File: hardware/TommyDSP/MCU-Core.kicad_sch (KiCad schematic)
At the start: 35 parts, among them SW201 SW_Push, SW202 SW_Push, U201 W25Q128JVS, U202 DNF, U203 RP2350_60QFN, Y1 ABM8-272-T3

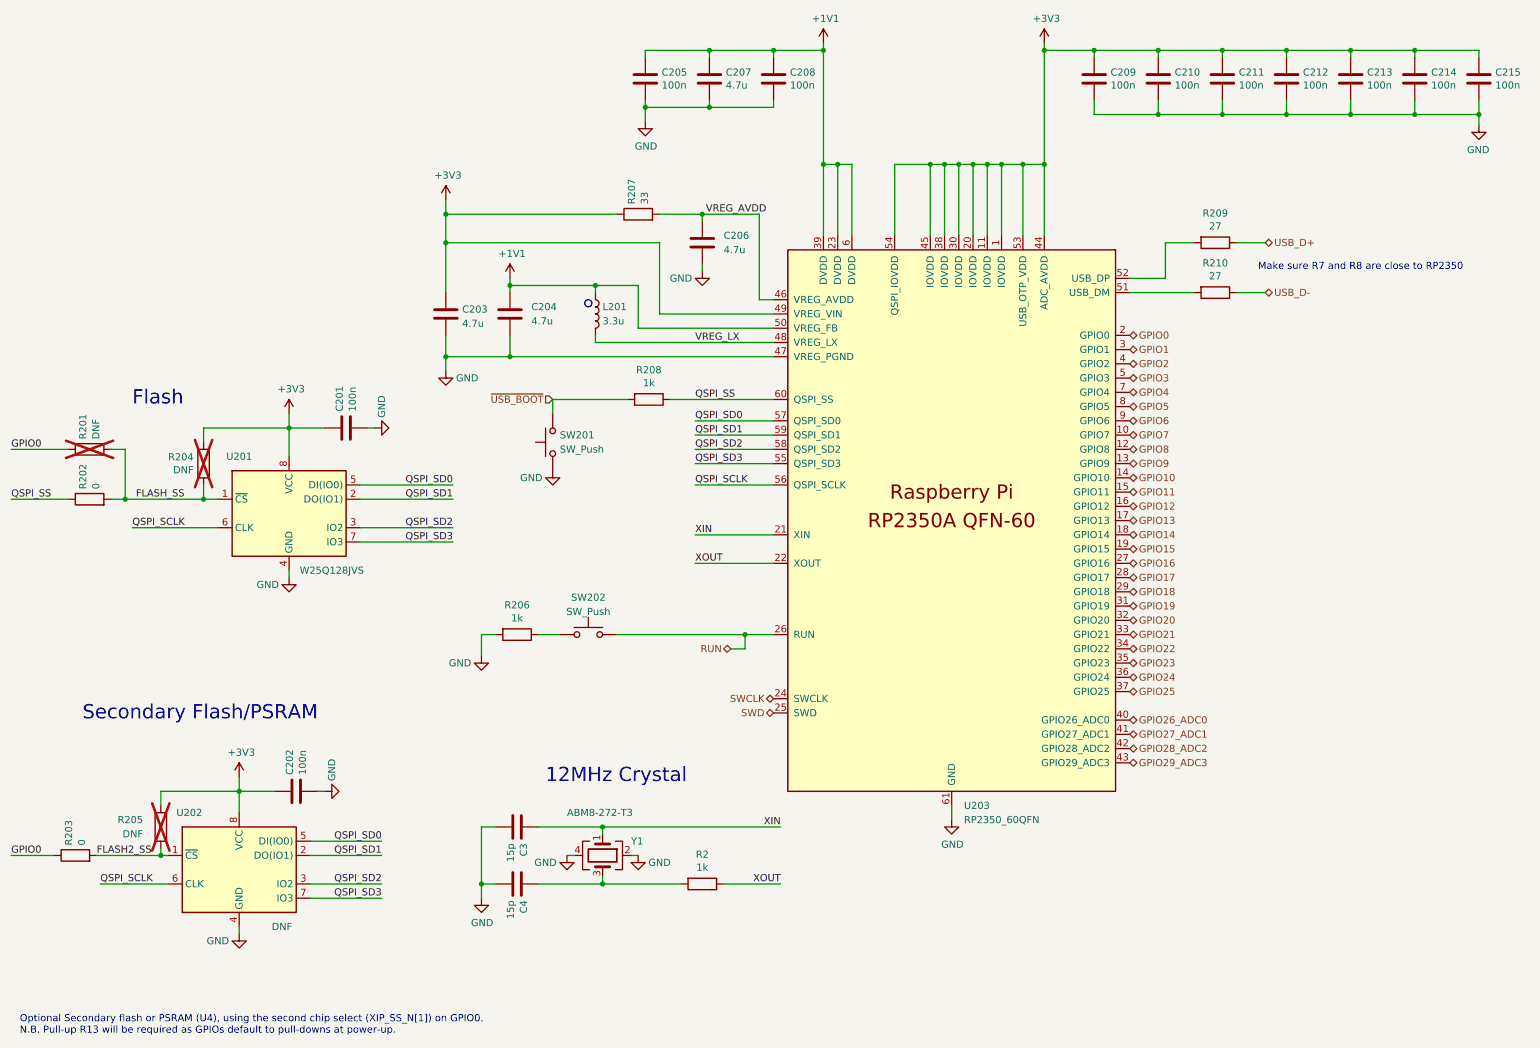
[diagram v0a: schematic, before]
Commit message: hardware: finished PCB routing
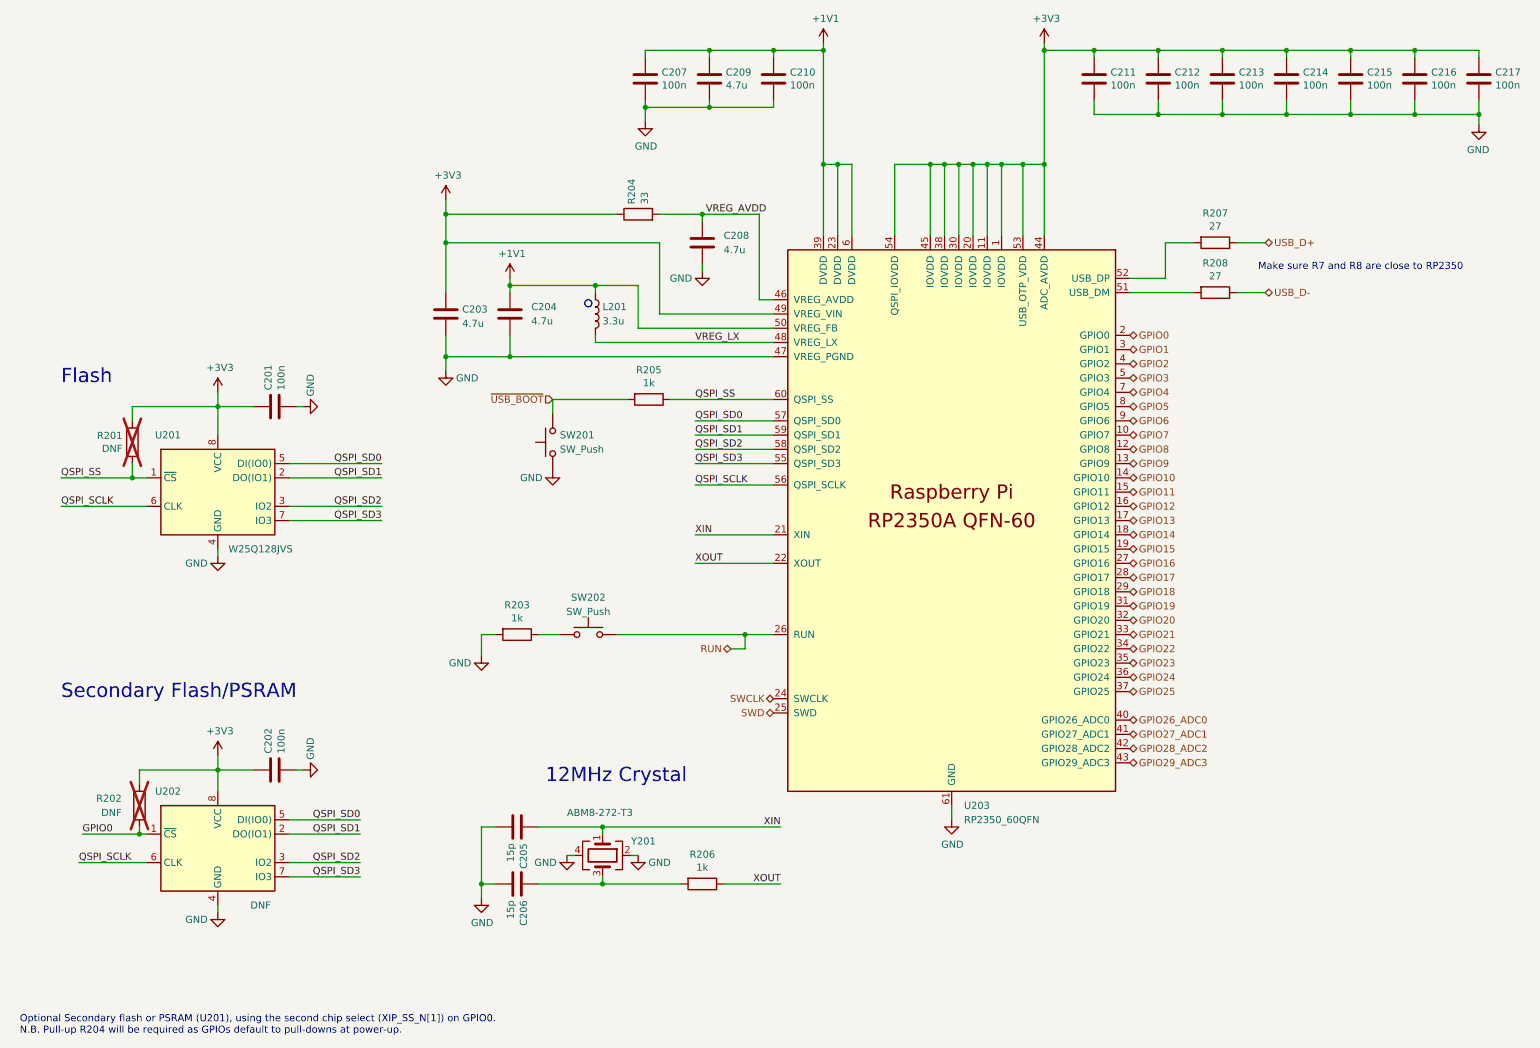
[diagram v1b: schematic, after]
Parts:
- removed R201: DNF, Resistor_SMD:R_0603_1608Metric, symbol Device:R
- removed R202, R203: 0, Resistor_SMD:R_0603_1608Metric, symbol Device:R
- C207: renamed from C205; footprint Capacitor_SMD:C_0603_1608Metric -> Capacitor_SMD:C_0402_1005Metric
- C209: renamed from C207; footprint Capacitor_SMD:C_0603_1608Metric -> Capacitor_SMD:C_0402_1005Metric
- C210: renamed from C208; footprint Capacitor_SMD:C_0603_1608Metric -> Capacitor_SMD:C_0402_1005Metric
- C211: renamed from C209; footprint Capacitor_SMD:C_0603_1608Metric -> Capacitor_SMD:C_0402_1005Metric
- C212: renamed from C210; footprint Capacitor_SMD:C_0603_1608Metric -> Capacitor_SMD:C_0402_1005Metric
- C213: renamed from C211; footprint Capacitor_SMD:C_0603_1608Metric -> Capacitor_SMD:C_0402_1005Metric
- C214: renamed from C212; footprint Capacitor_SMD:C_0603_1608Metric -> Capacitor_SMD:C_0402_1005Metric
- C215: renamed from C213; footprint Capacitor_SMD:C_0603_1608Metric -> Capacitor_SMD:C_0402_1005Metric
- C216: renamed from C214; footprint Capacitor_SMD:C_0603_1608Metric -> Capacitor_SMD:C_0402_1005Metric
- C217: renamed from C215; footprint Capacitor_SMD:C_0603_1608Metric -> Capacitor_SMD:C_0402_1005Metric
- renumbered C3 to C205, C4 to C206, C206 to C208, R204 to R201, R205 to R202, R206 to R203, R207 to R204, R208 to R205, R2 to R206, R209 to R207, R210 to R208, Y1 to Y201
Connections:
- net FLASH2_SS is gone; now on net GPIO0: R202.2, U202.1 (~{CS})
- net FLASH_SS is gone; now on net QSPI_SS: R201.2, U201.1 (~{CS})
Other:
- note added: "Optional Secondary flash or PSRAM (U201), using the second chip select (XIP_SS_N[1]) on GPIO0. N.B. Pull-up R204 will be required as GPIOs default to pull-downs at power-up."
- note removed: "Optional Secondary flash or PSRAM (U4), using the second chip select (XIP_SS_N[1]) on GPIO0. N.B. Pull-up R13 will be required as GPIOs default to pull-downs at power-up."
- title: (none) -> MCU Core
- moved on the sheet: C201, C202, R201, R202, U201, U202
